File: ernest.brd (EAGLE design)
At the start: 45 x 75 mm, 29 parts, among them IC1 ATMEGA328-P, SW1 IDENT, Y1 16MHz

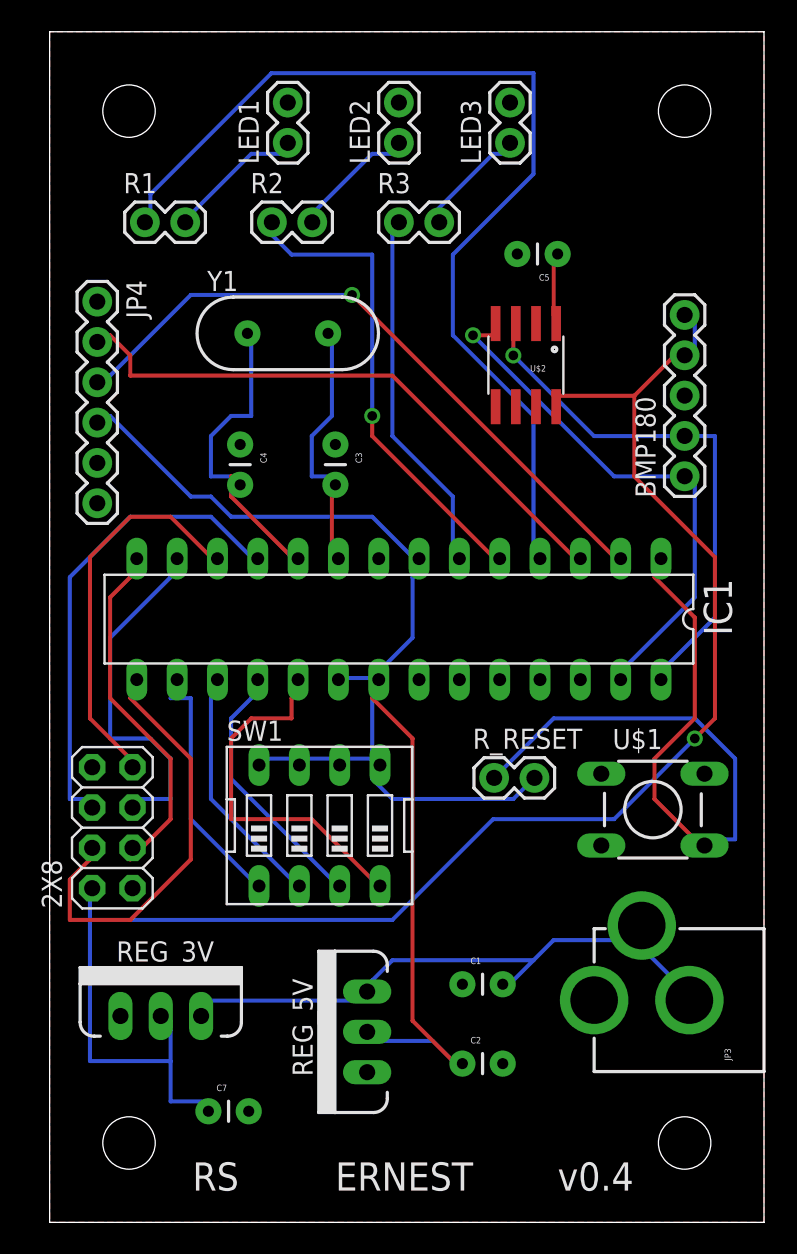
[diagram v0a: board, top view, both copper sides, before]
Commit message: Remove unnecessary 5v reg
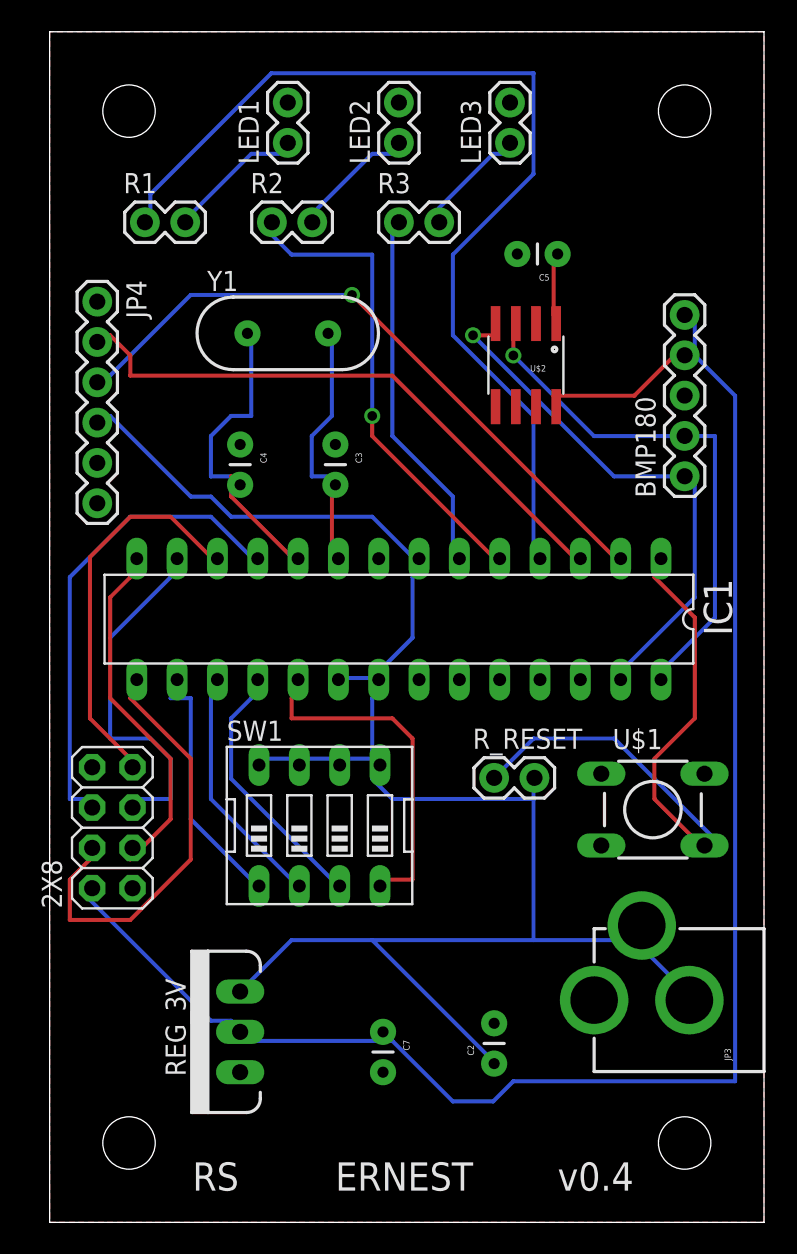
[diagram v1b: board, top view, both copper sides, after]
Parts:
- removed C1: 10uF, SparkFun-Capacitors:CAP-PTH-SMALL
- removed REG_5V: LM7805, User-Submitted:TO220V
- moved ERNEST 25.0 mm to (-5.00, -20.0)
- moved C7 12.1 mm to (21.0, 12.0), turned to 270 degrees
- moved REG_3V 5.10 mm to (12.0, 12.0), turned to 90 degrees
- moved C2 2.00 mm to (28.0, 10.0), turned to 90 degrees
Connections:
- removed net N$18: C1.2, JP3.GND, JP3.GNDBREAK, REG_3V.3, REG_5V.3
- net 5V: now also JP3.GND, JP3.GNDBREAK, REG_3V.3; no longer REG_5V.2
- net GND: no longer C1.1, REG_5V.1
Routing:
- net N$18: track 38.2 -> 0.00 mm
- net 5V: track 97.3 -> 116.5 mm
- net N$12: track 46.6 -> 40.0 mm
- net 3.3V: track 105.8 -> 108.6 mm, vias 1 -> 0

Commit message: Reorder SPI pins based off breadboard test
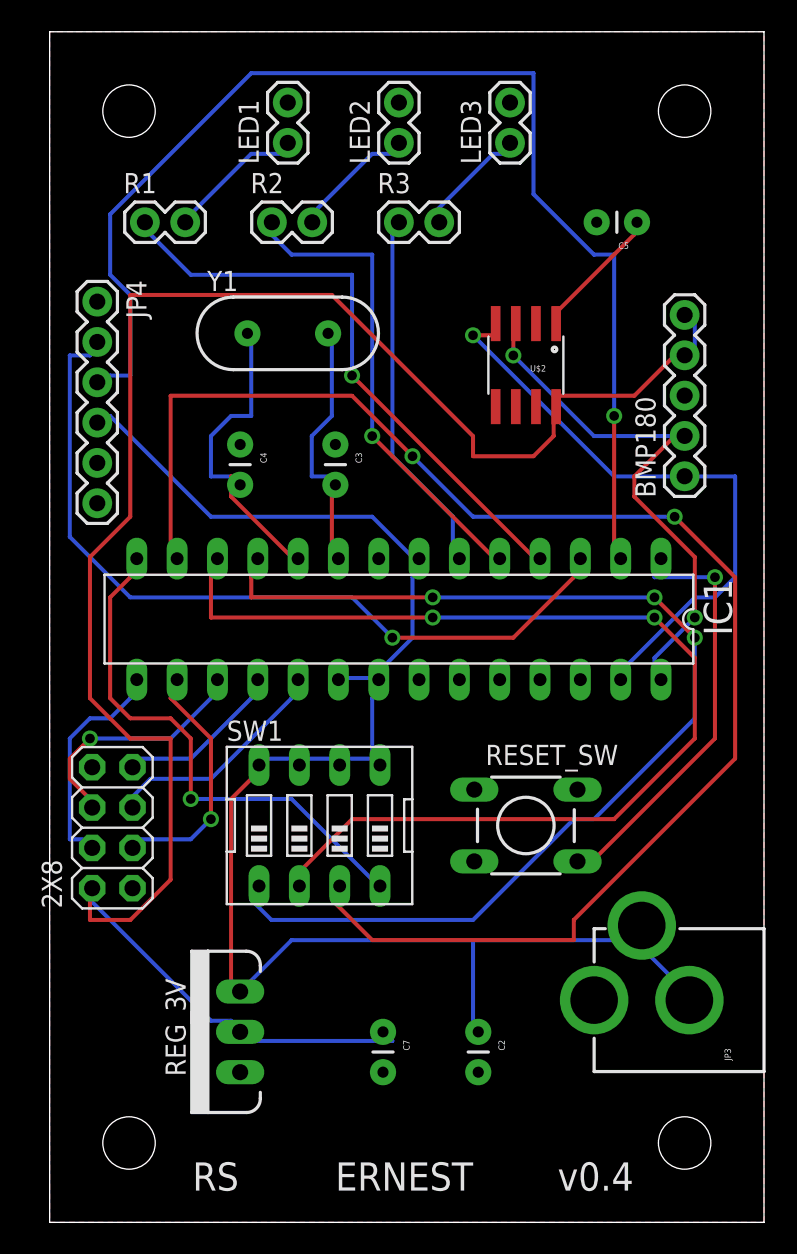
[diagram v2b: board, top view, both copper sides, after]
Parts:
- removed R_RESET: 10k, SparkFun-Connectors:1X02
- removed U$1: TACTILE-SWITCH-PTH, GeekAmmo:TAC-SWITCH-PTH
- added RESET_SW: SPST, GeekAmmo:TAC-SWITCH-PTH
- moved C5 5.39 mm to (37.0, 63.0)
- moved C2 2.24 mm to (27.0, 12.0), turned to 270 degrees
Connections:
- net 5V: no longer R_RESET.2
- net DIP_1: now also IC1.11; no longer IC1.16
- net DIP_2: now also IC1.12; no longer IC1.17
- net DIP_3: now also IC1.13; no longer IC1.18
- net DIP_4: now also IC1.14; no longer IC1.19
- net GND: now also RESET_SW.2; no longer U$1.2
- net MISO: now also IC1.18; no longer IC1.12
- net MOSI: now also IC1.17; no longer IC1.11
- net N$12: now also RESET_SW.4; no longer R_RESET.1, U$1.4
- net R_CE: now also IC1.16; no longer IC1.14
- net SCK: now also IC1.19; no longer IC1.13
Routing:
- net DIP_3: track 16.5 -> 95.2 mm, vias 0 -> 2
- net DIP_1: track 16.2 -> 71.3 mm, vias 0 -> 3
- net DIP_2: track 15.4 -> 70.1 mm, vias 0 -> 2
- net FTDI_TX: track 42.0 -> 77.0 mm
- net LED_OK: track 64.3 -> 37.5 mm, vias 0 -> 1
- net MOSI: track 30.3 -> 15.3 mm, vias 0 -> 1
- net FTDI_RX: track 37.1 -> 50.9 mm, vias 0 -> 1
- net MISO: track 24.5 -> 11.0 mm
- net 3.3V: track 108.6 -> 121.8 mm
- net N$12: track 40.0 -> 27.0 mm, vias 0 -> 1
- net R_CSN: track 27.3 -> 14.3 mm
- net 5V: track 116.5 -> 104.6 mm
- net DIP_4: track 22.7 -> 33.5 mm, vias 0 -> 1
- net SCK: track 23.0 -> 14.6 mm
- net R_CE: track 22.9 -> 16.1 mm, vias 0 -> 1
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
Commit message: V0.4 release
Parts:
- removed ERNEST: Ernest, SparkFun-Aesthetics:CREATIVE_COMMONS
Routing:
- net DIP_3: track 95.2 -> 90.0 mm, vias 2 -> 3
- net 5V: track 104.6 -> 101.8 mm
- net DIP_1: track 71.3 -> 68.6 mm
- net R_CE: track 16.1 -> 14.6 mm
- net DIP_2: track 70.1 -> 69.4 mm, vias 2 -> 3
- net DIP_4: track 33.5 -> 34.2 mm, vias 1 -> 0
